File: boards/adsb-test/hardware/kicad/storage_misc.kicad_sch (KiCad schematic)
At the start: 20 parts, among them J1501 microSD (push-pull, detect), Q1501 AO3401A, U1501 TCA6408APW

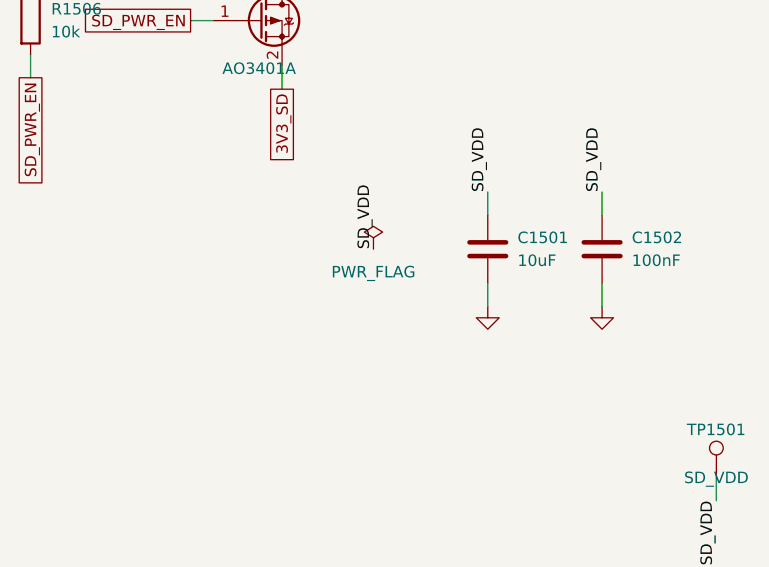
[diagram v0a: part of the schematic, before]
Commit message: ADSB_Test: User USB-C on its own sheet, RP2040 GPIO header + optional I2C, shunt/PWR_FLAG text fixed
Co-Authored-By: Claude Opus 5.5 <noreply@anthropic.com>
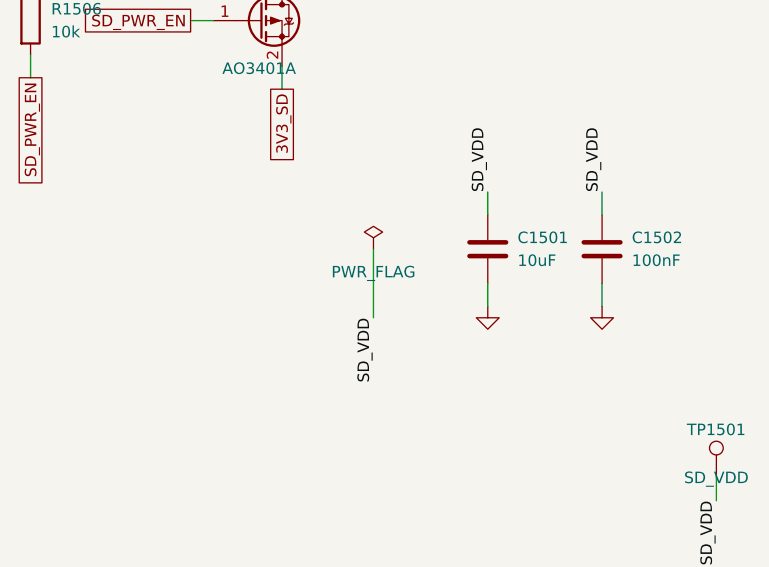
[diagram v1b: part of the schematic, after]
